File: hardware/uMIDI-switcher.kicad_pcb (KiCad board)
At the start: 2 copper layers, 127 x 50 mm, 104 parts, among them Q1 BSS138, Q2 BSS138, Q3 BSS138, Q4 BSS138, Q5 BSS138, Q6 BSS138, Q7 BSS138, Q8 BSS138, U1 MC7809CD, U2 MC7809CD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

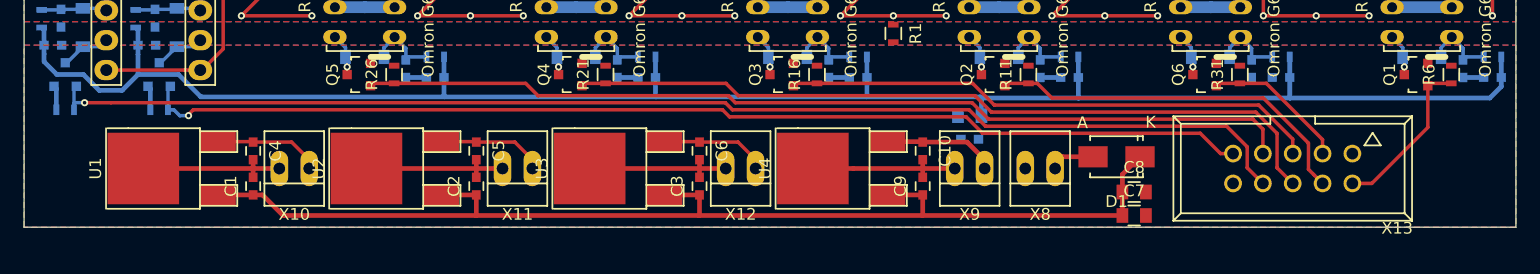
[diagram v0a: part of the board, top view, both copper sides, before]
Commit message: Use new ldo footprint; Adapt placement
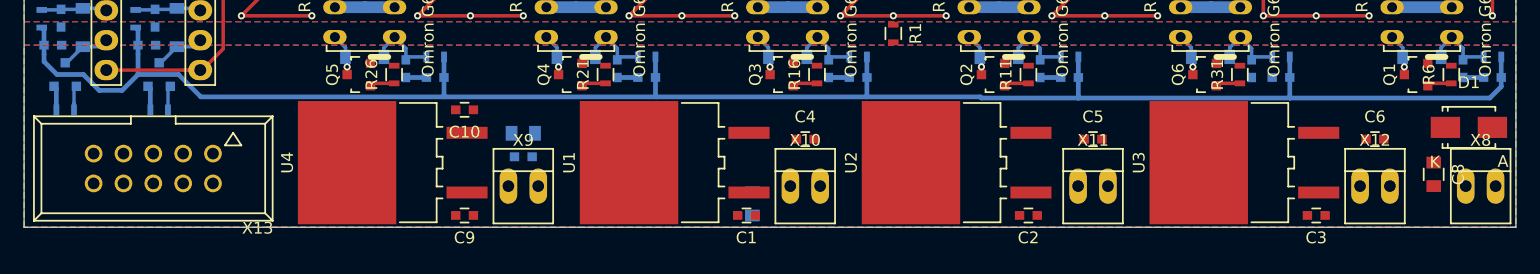
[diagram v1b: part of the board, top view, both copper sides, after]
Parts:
- C7: moved to B.Cu
- U1, U2, U3, U4: footprint TO_SOT_Packages_SMD:TO-252-2Lead -> uMIDI-switcher:D2PAK-3
- X8: value CONN_01X02 -> 12V in
- moved X13 97.0 mm to (88.5, 124.0)
- moved C6 57.5 mm to (192.5, 121.5), turned to 0 degrees
- moved X12 54.0 mm to (192.5, 125.5), turned to 0 degrees
- moved C3 52.6 mm to (187.5, 128.0), turned to 180 degrees
- moved C5 52.5 mm to (168.5, 121.5), turned to 0 degrees
- moved X11 49.0 mm to (168.5, 125.5), turned to 0 degrees
- moved C2 47.1 mm to (163.0, 128.0), turned to 180 degrees
- moved C4 47.0 mm to (144.0, 121.5), turned to 0 degrees
- moved U4 46.0 mm to (105.0, 123.5)
- moved U3 45.5 mm to (177.5, 123.5)
- moved X10 43.5 mm to (144.0, 125.5), turned to 0 degrees
- moved C1 42.1 mm to (139.0, 128.0), turned to 180 degrees
- moved U2 40.0 mm to (153.0, 123.5)
- moved C10 39.2 mm to (115.0, 119.0), turned to 180 degrees
- moved C9 39.1 mm to (115.0, 128.0), turned to 180 degrees
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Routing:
- net /Switch1/Ctrl: track 107.2 -> 2.08 mm, vias 1 -> 0
- net +12V: track 97.7 -> 0.00 mm
- net /Switch2/Ctrl: track 94.8 -> 2.08 mm, vias 1 -> 0
- net /Looper5/Ctrl: track 79.7 -> 2.08 mm
- net /Looper4/Ctrl: track 65.8 -> 2.08 mm
- net GND: track 65.7 -> 12.9 mm
- net /Looper3/Ctrl: track 45.8 -> 2.08 mm
- net /Looper2/Ctrl: track 32.0 -> 2.08 mm
- net /Tuner/Ctrl: track 14.0 -> 2.08 mm
- net +9V: track 164.9 -> 153.7 mm
- net /Looper1/Ctrl: track 12.3 -> 2.08 mm
- net Net-(C6-Pad1): track 9.16 -> 0.00 mm
- net Net-(C5-Pad1): track 9.16 -> 0.00 mm
- net Net-(C4-Pad1): track 9.16 -> 0.00 mm
- net /pwr_in: track 3.86 -> 0.00 mm

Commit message: Place and route
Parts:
- C11, C12: moved to F.Cu
- Q1, Q2, Q3, Q4, Q5, Q6, R11, R16, R21, R26, R31, R6: moved to B.Cu
- moved R11 9.06 mm to (154.0, 115.0)
- moved R16 9.06 mm to (136.0, 115.0)
- moved R21 9.06 mm to (118.0, 115.0)
- moved R26 9.06 mm to (100.0, 115.0)
- moved R31 9.06 mm to (172.0, 115.0)
- moved R6 9.06 mm to (190.0, 115.0)
- moved C5 6.04 mm to (163.0, 119.0), turned to 180 degrees
- moved C4 5.59 mm to (139.0, 119.0), turned to 180 degrees
- moved C6 5.59 mm to (187.5, 119.0), turned to 180 degrees
- moved Q1 3.64 mm to (192.5, 115.0)
- moved Q2 3.64 mm to (156.5, 115.0)
- moved Q3 3.64 mm to (138.5, 115.0)
- moved Q4 3.64 mm to (120.5, 115.0)
- moved Q5 3.64 mm to (102.5, 115.0)
- moved Q6 3.64 mm to (174.5, 115.0)
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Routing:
- net /Tuner/Ctrl: track 2.08 -> 101.2 mm, vias 0 -> 1
- net +12V: track 0.00 -> 97.4 mm, vias 0 -> 2
- net /Looper1/Ctrl: track 2.08 -> 84.3 mm, vias 0 -> 1
- net /Looper2/Ctrl: track 2.08 -> 70.5 mm, vias 0 -> 1
- net /Looper3/Ctrl: track 2.08 -> 51.1 mm, vias 0 -> 1
- net /Looper4/Ctrl: track 2.08 -> 38.2 mm, vias 0 -> 1
- net /Looper5/Ctrl: track 2.08 -> 17.6 mm, vias 0 -> 1
- net /Switch1/Ctrl: track 2.08 -> 11.1 mm
- net +9V: track 153.7 -> 162.0 mm
- net /Switch2/Ctrl: track 2.08 -> 10.4 mm
- net /pwr_in: track 0.00 -> 6.14 mm
- net Net-(C6-Pad1): track 0.00 -> 2.18 mm
- net Net-(C5-Pad1): track 0.00 -> 2.18 mm
- net Net-(C4-Pad1): track 0.00 -> 2.18 mm
- net /Looper5/Single True Bypass/relais_n: track 3.62 -> 2.26 mm, vias 1 -> 0
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
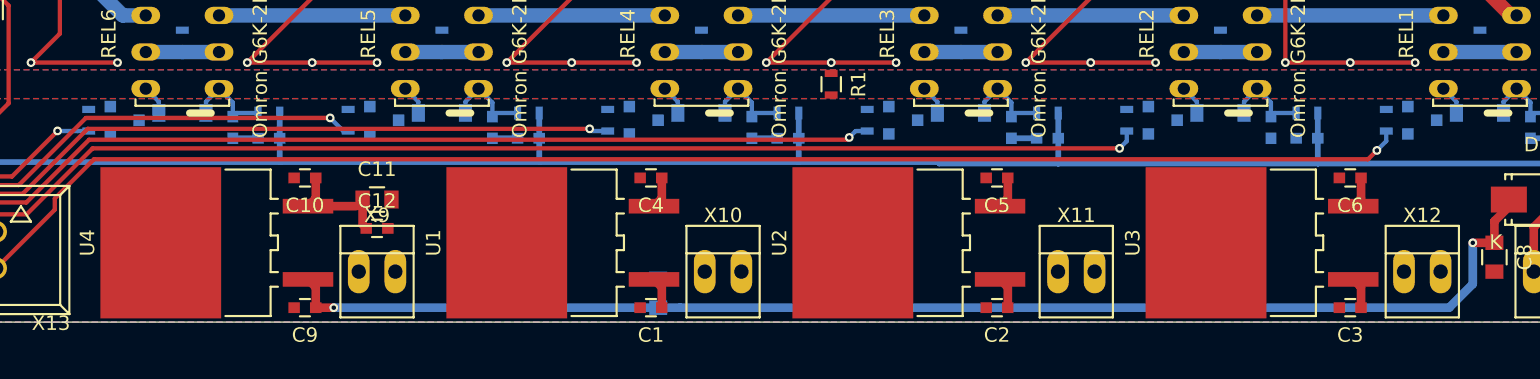
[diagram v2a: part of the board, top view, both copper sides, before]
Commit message: Add 10uF caps to 9V outputs; Place and route
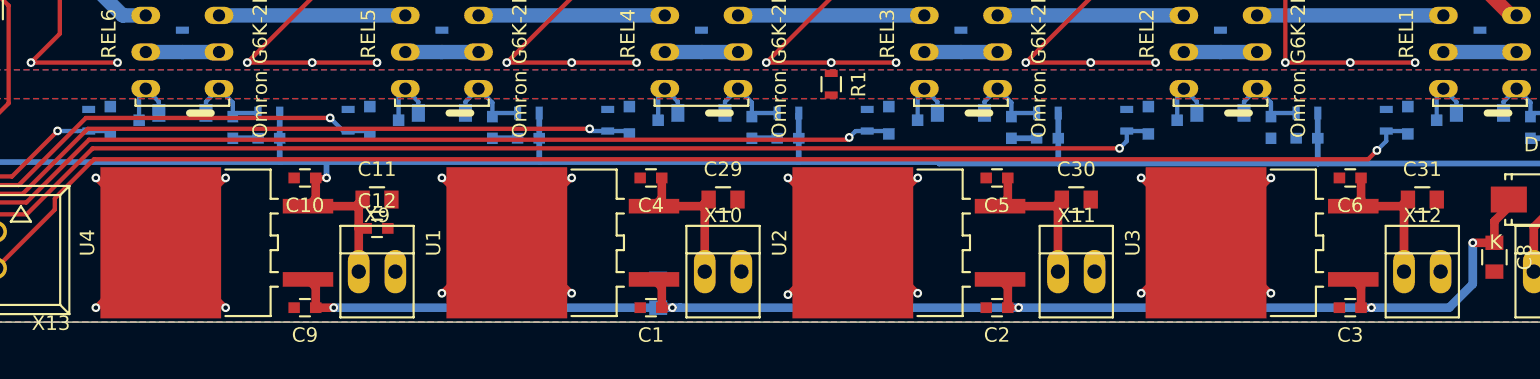
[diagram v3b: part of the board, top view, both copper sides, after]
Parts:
- added C29: 10u, Capacitors_SMD:C_0805, F.Cu at (144.0, 120.5)
- added C30: 10u, Capacitors_SMD:C_0805, F.Cu at (168.5, 120.5)
- added C31: 10u, Capacitors_SMD:C_0805, F.Cu at (192.5, 120.5)
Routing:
- net GND: track 12.9 -> 112.3 mm, vias 0 -> 16
- net Net-(C30-Pad1): track 2.18 -> 11.8 mm
- net Net-(C31-Pad1): track 2.18 -> 11.3 mm
- net Net-(C29-Pad1): track 2.18 -> 11.3 mm
- net +9V: track 162.0 -> 167.4 mm, vias 0 -> 1
- net /Tuner/relais_n: track 2.26 -> 4.64 mm
- net /Looper3/Single True Bypass/relais_n: track 2.26 -> 4.64 mm
- net /Looper2/Single True Bypass/relais_n: track 2.26 -> 4.64 mm
- net /Looper1/Single True Bypass/relais_n: track 2.26 -> 4.64 mm
- net /Looper5/Single True Bypass/relais_n: track 2.26 -> 4.64 mm
- net /Looper4/Single True Bypass/relais_n: track 2.26 -> 4.64 mm
- net +12V: track 97.4 -> 99.6 mm, vias 2 -> 5
- net /Looper4/Ctrl: track 38.2 -> 39.8 mm
- net /Looper5/Ctrl: track 17.6 -> 19.1 mm
- net /Looper3/Ctrl: track 51.1 -> 52.7 mm
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
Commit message: Finish routing
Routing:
- net GND: track 112.3 -> 218.8 mm, vias 16 -> 54
- net GNDA: track 151.0 -> 179.2 mm, vias 18 -> 22
- net /Tuner/bypass: track 5.08 -> 7.63 mm
- net /Looper3/Ctrl: track 52.7 -> 54.1 mm
- net /Looper4/Ctrl: track 39.8 -> 40.5 mm

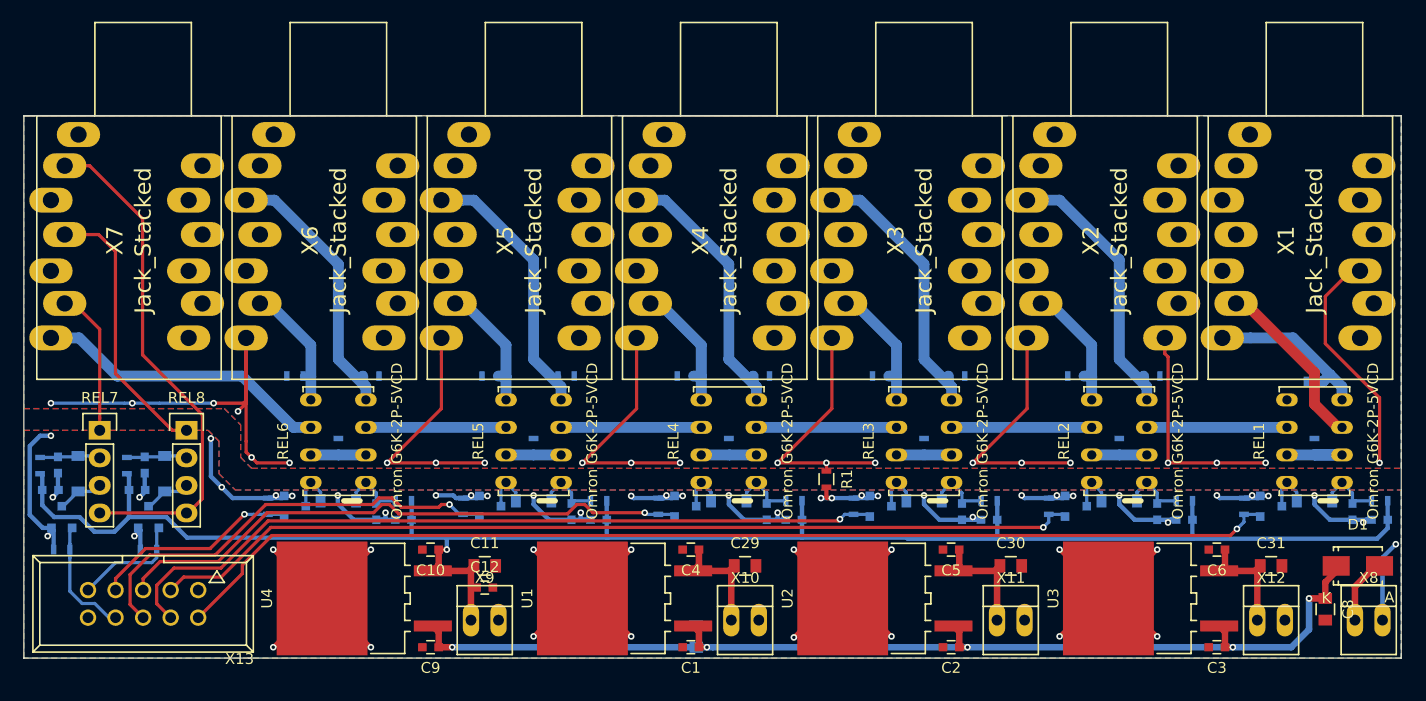
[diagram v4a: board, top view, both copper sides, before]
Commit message: Revise pcb (and some footprints) silk screen
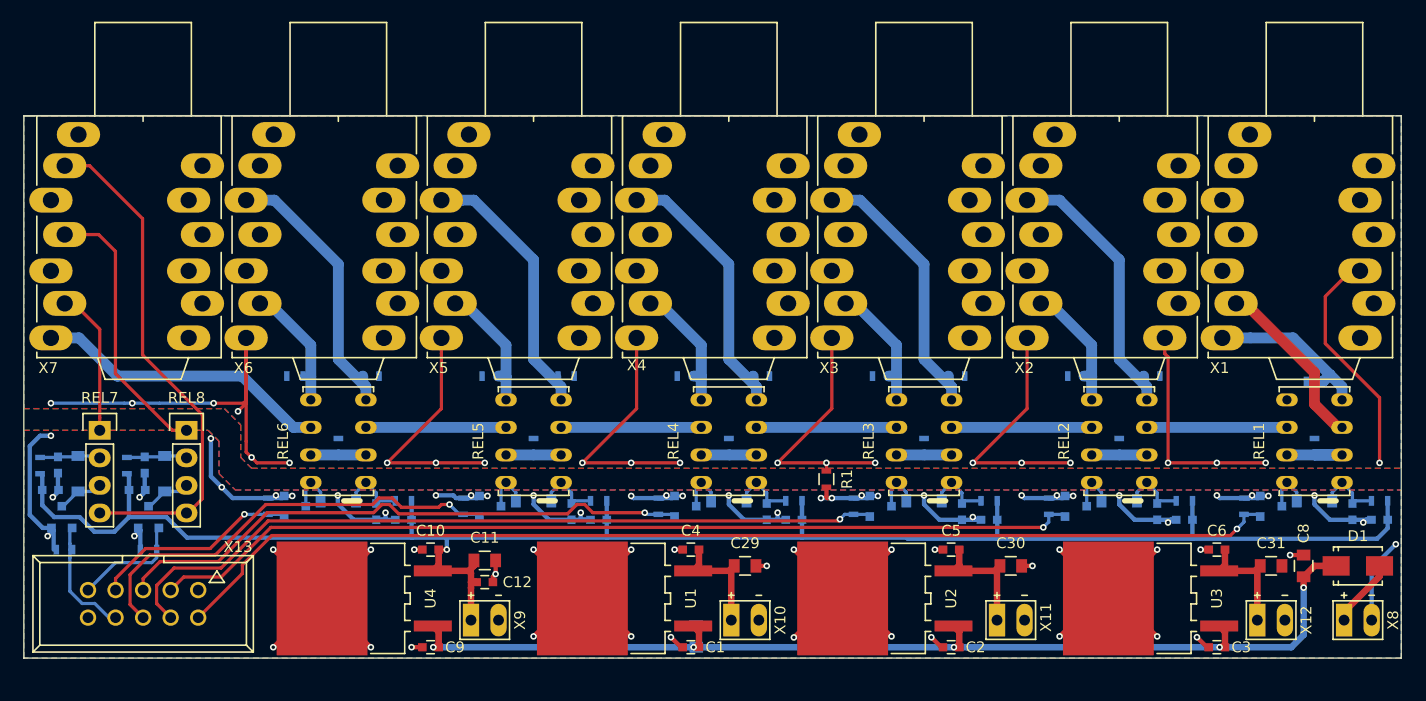
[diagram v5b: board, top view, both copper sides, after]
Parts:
- X10, X11, X12, X8, X9: footprint Connect:PINHEAD1-2 -> uMIDI-switcher:PINHEAD-Supply
- moved C8 4.47 mm to (195.5, 120.5), turned to 90 degrees
- moved X8 1.00 mm to (200.5, 125.5)
- moved C11 0.50 mm to (120.0, 120.0)
- moved C12 0.50 mm to (120.0, 122.0)
- moved R33 0.25 mm to (81.2, 119.0)
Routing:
- net GND: track 218.8 -> 233.0 mm, vias 54 -> 66
- net /pwr_in: track 6.14 -> 6.70 mm
- net +12V: track 99.6 -> 100.2 mm

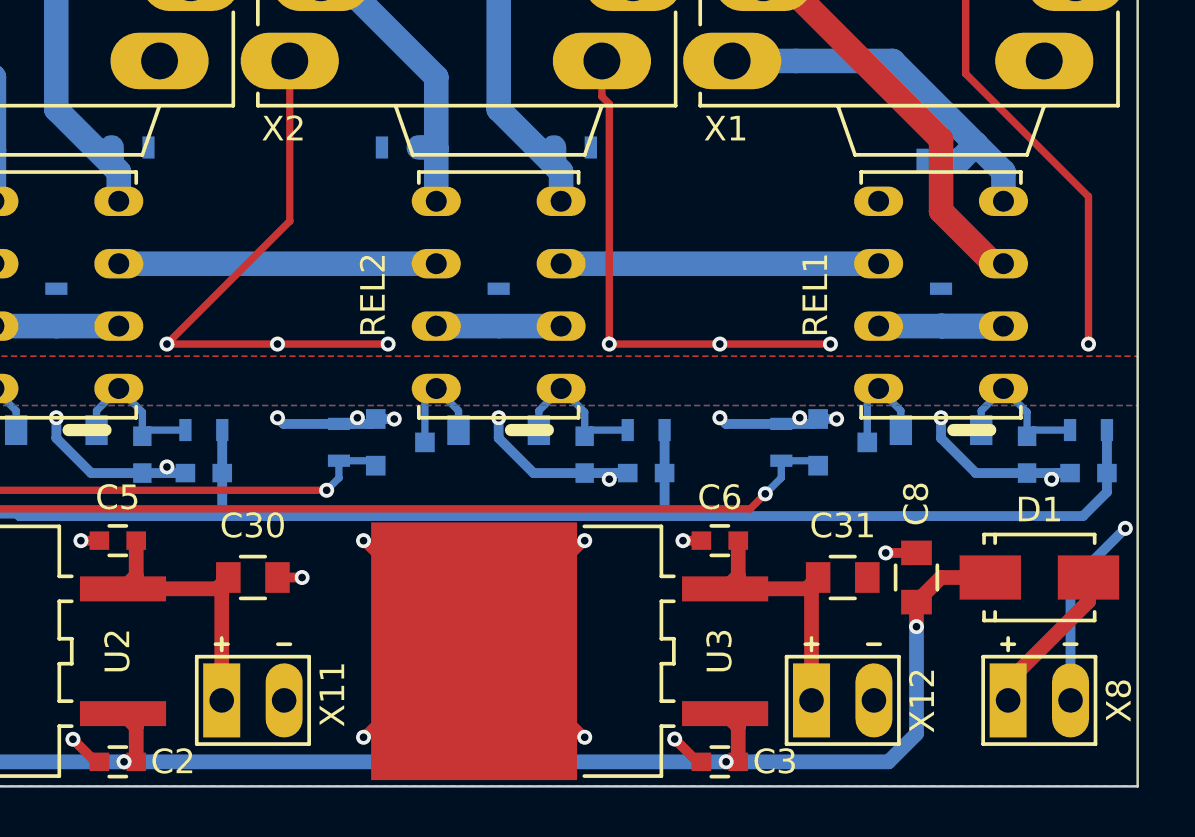
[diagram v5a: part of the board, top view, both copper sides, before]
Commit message: Revise bottom silk screen; DRC clean
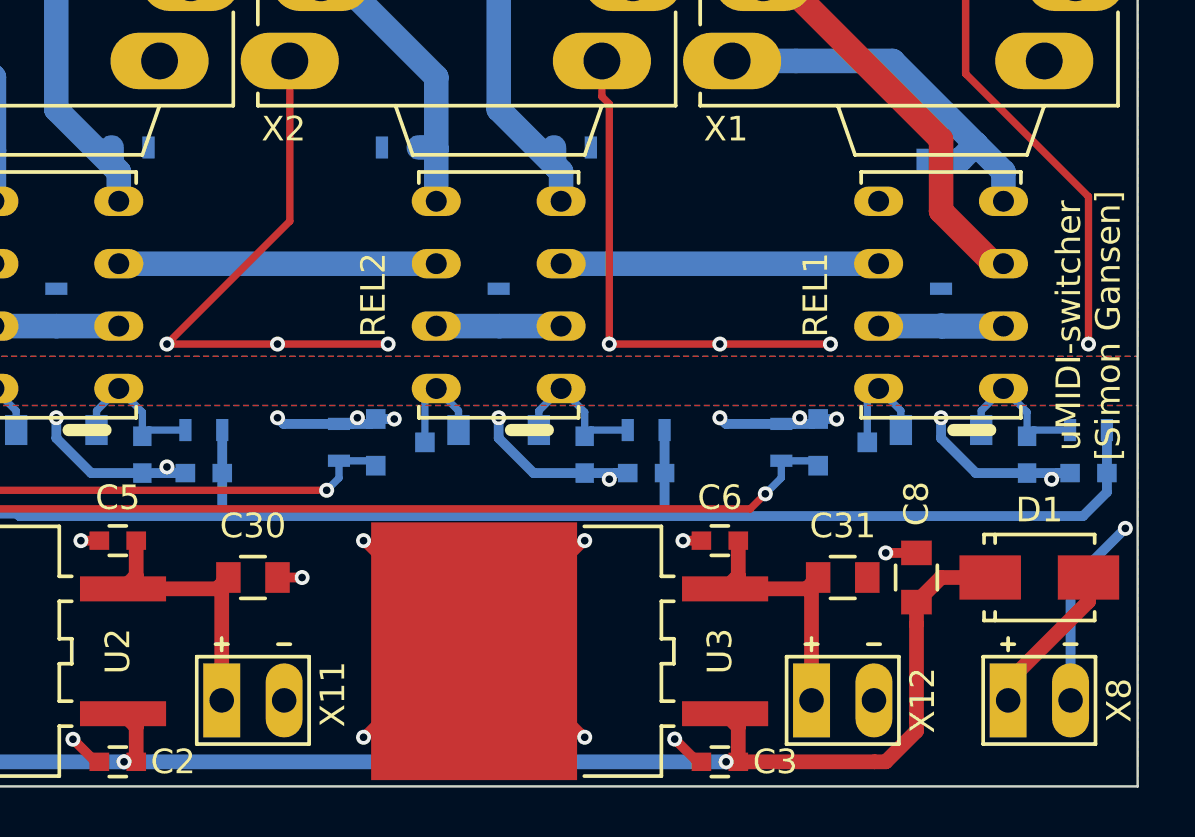
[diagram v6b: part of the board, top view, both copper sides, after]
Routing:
- net +12V: vias 5 -> 4
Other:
- board text added: "uMIDI-switcher [Simon Gansen]"
